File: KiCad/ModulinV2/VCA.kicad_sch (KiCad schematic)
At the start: 9 parts, among them IC20 AS3360D, U8 TL072HIDR

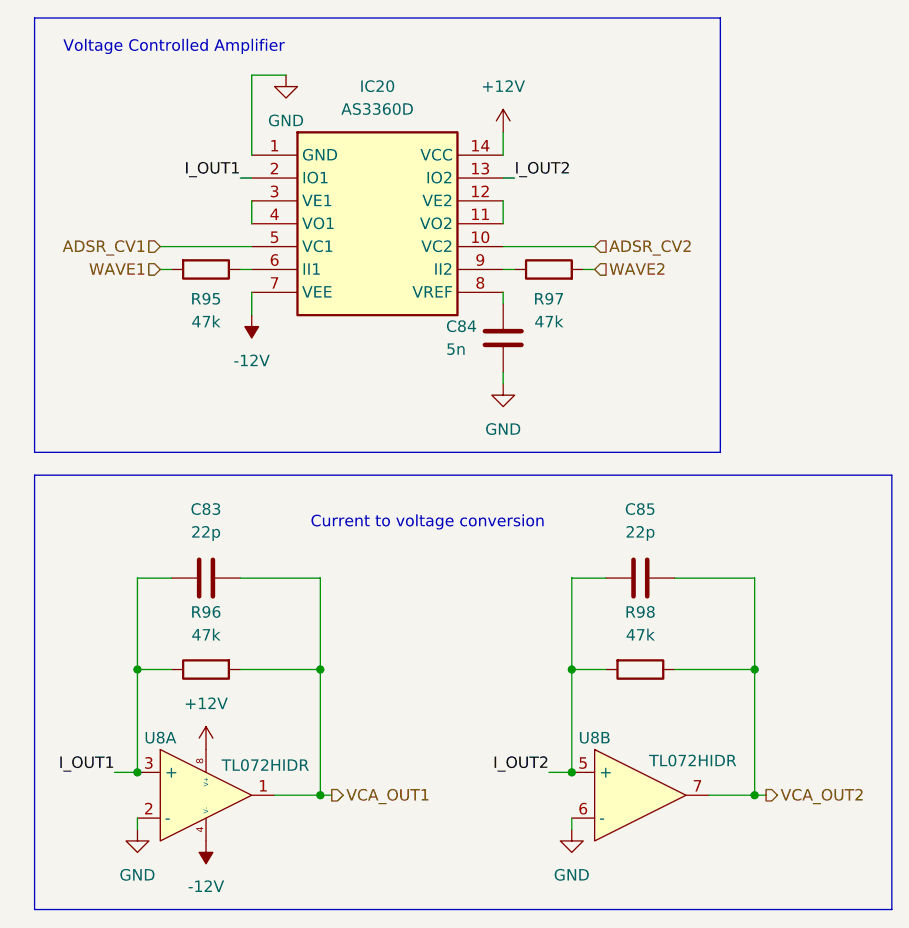
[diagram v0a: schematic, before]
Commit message: Fixed library issues and assigned most footprints
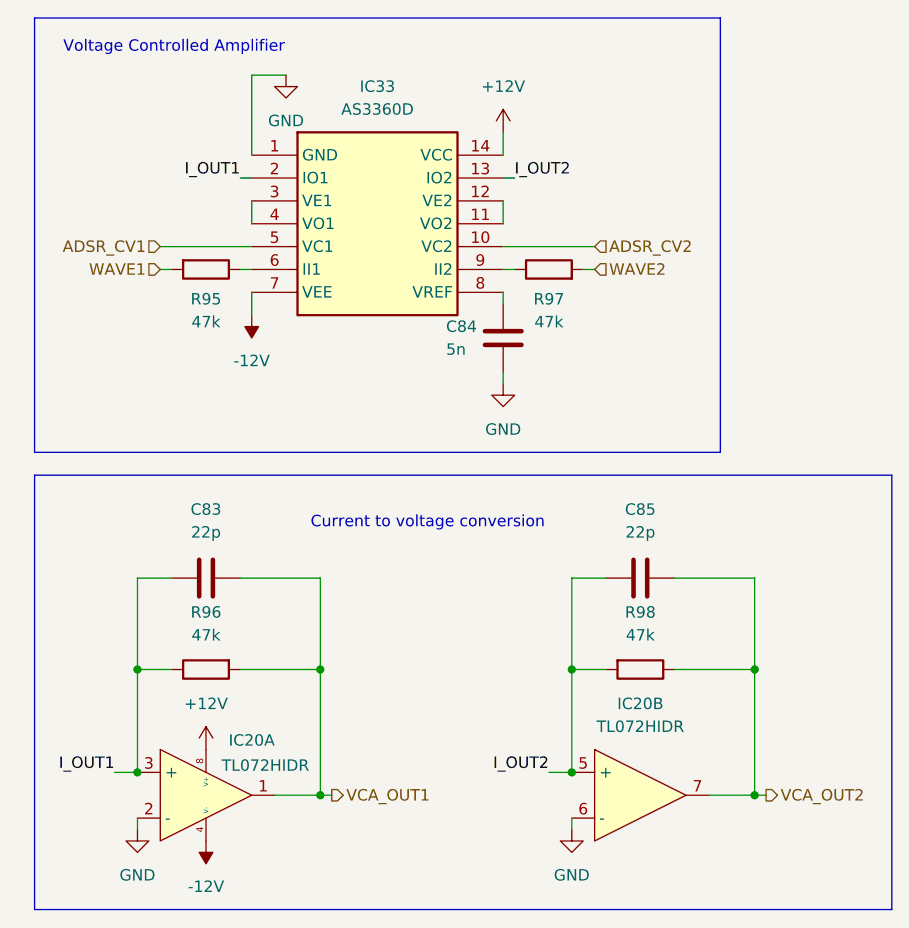
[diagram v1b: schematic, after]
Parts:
- removed IC20: AS3360D, SOIC127P620X175-14N, symbol AS3360D:AS3360D
- removed U8: TL072HIDR, symbol TL072HIDR:TL072HIDRx2
- added IC20: TL072HIDR, SamacSys_Parts:SOIC127P600X175-8N, symbol SamacSys_Parts:TL072HIDR
- added IC33: AS3360D, SamacSys_Parts:SOIC127P620X175-14N, symbol SamacSys_Parts:AS3360D
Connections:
- net +12V: now also IC20.8 (V+), IC33.14 (VCC)
- net -12V: now also IC20.4 (V-), IC33.7 (VEE)
- net ADSR_CV1: now also IC33.5 (VC1)
- net ADSR_CV2: now also IC33.10 (VC2)
- net GND: now also IC20.2 (-), IC20.6 (-), IC33.1 (GND)
- net I_OUT1: now also IC20.3 (+), IC33.2 (IO1)
- net I_OUT2: now also IC20.5 (+), IC33.13 (IO2)
- net VCA_OUT1: now also IC20.1
- net VCA_OUT2: now also IC20.7
- net at R97.1: now also IC33.9 (II2)
- net at R95.1: now also IC33.6 (II1)
- net at C84.1: now also IC33.8 (VREF)
- new net: IC33.11 (VO2), IC33.12 (VE2)
- new net: IC33.3 (VE1), IC33.4 (VO1)

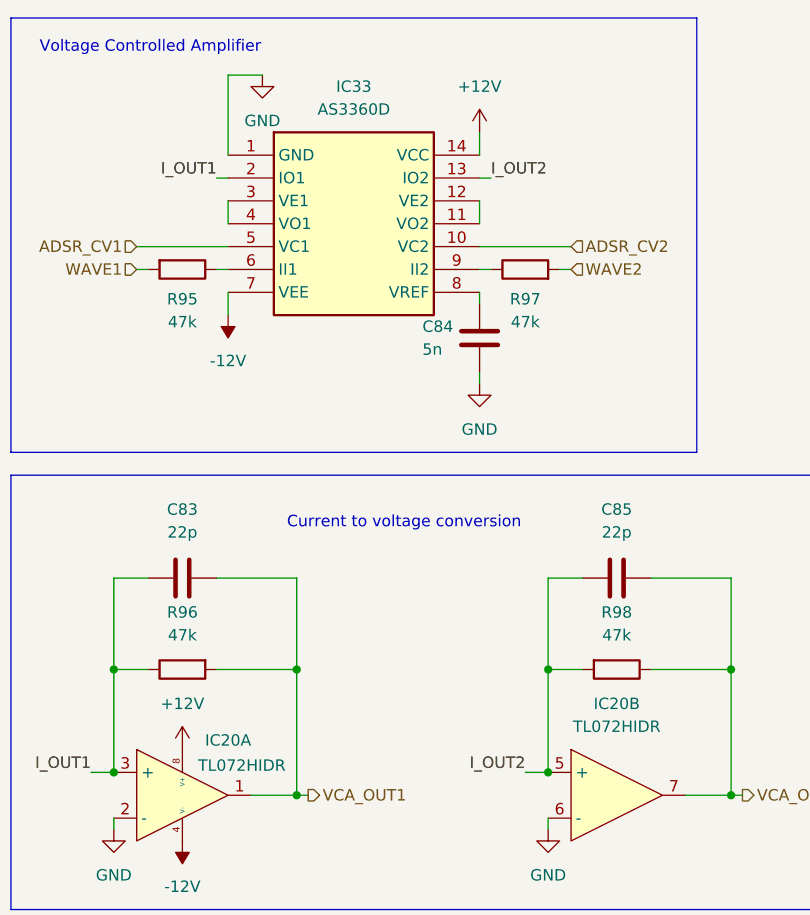
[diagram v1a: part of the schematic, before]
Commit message: Changed switch for the boot and nrst. Fixed the GATE interface trigger
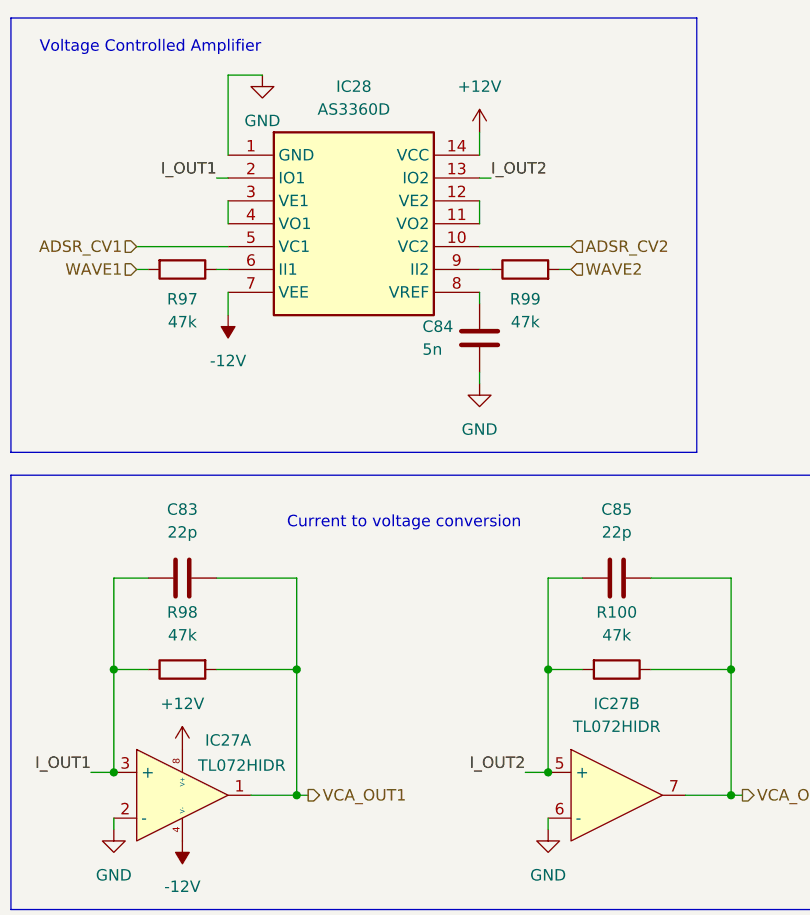
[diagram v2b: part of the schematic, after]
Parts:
- renumbered IC20 to IC27, IC33 to IC28, R98 to R100, R95 to R97, R96 to R98, R97 to R99
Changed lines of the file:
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@@
 		(dnp no)
 		(fields_autoplaced yes)
-		(property "Reference" "R98"
+		(property "Reference" "R100"
 			(at 81.28 80.01 90)
 			(effects
@@
 			(project "ModulinV2"
 				(path "/c6b34a57-3941-4b56-8b80-1848c7f41082/a5a8abcc-50bb-4382-96d0-cbdb724bb6e9"
-					(reference "R98")
+					(reference "R100")
 					(unit 1)
 				)
@@
 		(dnp no)
 		(fields_autoplaced yes)
-		(property "Reference" "#PWR0196"
+		(property "Reference" "#PWR0204"
 			(at 66.04 30.48 0)
 			(effects
@@
 			(project ""
 				(path "/c6b34a57-3941-4b56-8b80-1848c7f41082/a5a8abcc-50bb-4382-96d0-cbdb724bb6e9"
-					(reference "#PWR0196")
+					(reference "#PWR0204")
 					(unit 1)
 				)
@@
 		(on_board yes)
 		(dnp no)
-		(property "Reference" "R97"
+		(property "Reference" "R99"
 			(at 71.12 45.212 90)
 			(effects
@@
 			(project "ModulinV2"
 				(path "/c6b34a57-3941-4b56-8b80-1848c7f41082/a5a8abcc-50bb-4382-96d0-cbdb724bb6e9"
-					(reference "R97")
+					(reference "R99")
 					(unit 1)
 				)
@@
 		(dnp no)
 		(fields_autoplaced yes)
-		(property "Reference" "#PWR0192"
+		(property "Reference" "#PWR0200"
 			(at 33.02 99.06 0)
 			(effects
@@
 			(project "ModulinV2"
 				(path "/c6b34a57-3941-4b56-8b80-1848c7f41082/a5a8abcc-50bb-4382-96d0-cbdb724bb6e9"
-					(reference "#PWR0192")
+					(reference "#PWR0200")
 					(unit 1)
 				)
@@
 		(on_board yes)
 		(dnp no)
-		(property "Reference" "R95"
+		(property "Reference" "R97"
 			(at 33.02 45.212 90)
 			(effects
@@
 			(project "ModulinV2"
 				(path "/c6b34a57-3941-4b56-8b80-1848c7f41082/a5a8abcc-50bb-4382-96d0-cbdb724bb6e9"
-					(reference "R95")
+					(reference "R97")
 					(unit 1)
 				)
@@
 		(dnp no)
 		(fields_autoplaced yes)
-		(property "Reference" "#PWR0191"
+		(property "Reference" "#PWR0199"
 			(at 25.4 110.49 0)
 			(effects
@@
 			(project ""
 				(path "/c6b34a57-3941-4b56-8b80-1848c7f41082/a5a8abcc-50bb-4382-96d0-cbdb724bb6e9"
-					(reference "#PWR0191")
+					(reference "#PWR0199")
 					(unit 1)
 				)
@@
 		(dnp no)
 		(fields_autoplaced yes)
-		(property "Reference" "#PWR0197"
+		(property "Reference" "#PWR0205"
 			(at 66.04 60.96 0)
 			(effects
@@
 			(project ""
 				(path "/c6b34a57-3941-4b56-8b80-1848c7f41082/a5a8abcc-50bb-4382-96d0-cbdb724bb6e9"
-					(reference "#PWR0197")
+					(reference "#PWR0205")
 					(unit 1)
 				)
@@
 		(dnp no)
 		(fields_autoplaced yes)
-		(property "Reference" "#PWR0194"
+		(property "Reference" "#PWR0202"
 			(at 38.1 43.18 0)
 			(effects
@@
 			(project ""
 				(path "/c6b34a57-3941-4b56-8b80-1848c7f41082/a5a8abcc-50bb-4382-96d0-cbdb724bb6e9"
-					(reference "#PWR0194")
+					(reference "#PWR0202")
 					(unit 1)
 				)
@@
 		(dnp no)
 		(fields_autoplaced yes)
-		(property "Reference" "IC20"
+		(property "Reference" "IC27"
 			(at 81.28 90.17 0)
 			(effects
@@
 			(project ""
 				(path "/c6b34a57-3941-4b56-8b80-1848c7f41082/a5a8abcc-50bb-4382-96d0-cbdb724bb6e9"
-					(reference "IC20")
+					(reference "IC27")
 					(unit 2)
 				)
@@
 		(dnp no)
 		(fields_autoplaced yes)
-		(property "Reference" "#PWR0195"
+		(property "Reference" "#PWR0203"
 			(at 41.91 26.67 0)
 			(effects
@@
 			(project ""
 				(path "/c6b34a57-3941-4b56-8b80-1848c7f41082/a5a8abcc-50bb-4382-96d0-cbdb724bb6e9"
-					(reference "#PWR0195")
+					(reference "#PWR0203")
 					(unit 1)
 				)
@@
 		(dnp no)
 		(fields_autoplaced yes)
-		(property "Reference" "R96"
+		(property "Reference" "R98"
 			(at 33.02 80.01 90)
 			(effects
@@
 			(project ""
 				(path "/c6b34a57-3941-4b56-8b80-1848c7f41082/a5a8abcc-50bb-4382-96d0-cbdb724bb6e9"
-					(reference "R96")
+					(reference "R98")
 					(unit 1)
 				)
@@
 		(dnp no)
 		(fields_autoplaced yes)
-		(property "Reference" "IC33"
+		(property "Reference" "IC28"
 			(at 52.07 21.59 0)
 			(effects
@@
 			(project ""
 				(path "/c6b34a57-3941-4b56-8b80-1848c7f41082/a5a8abcc-50bb-4382-96d0-cbdb724bb6e9"
-					(reference "IC33")
+					(reference "IC28")
 					(unit 1)
 				)
@@
 		(on_board yes)
 		(dnp no)
-		(property "Reference" "IC20"
+		(property "Reference" "IC27"
 			(at 38.1 94.234 0)
 			(effects
@@
 			(project ""
 				(path "/c6b34a57-3941-4b56-8b80-1848c7f41082/a5a8abcc-50bb-4382-96d0-cbdb724bb6e9"
-					(reference "IC20")
+					(reference "IC27")
 					(unit 1)
 				)
@@
 		(dnp no)
 		(fields_autoplaced yes)
-		(property "Reference" "#PWR0193"
+		(property "Reference" "#PWR0201"
 			(at 33.02 101.6 0)
 			(effects
@@
 			(project "ModulinV2"
 				(path "/c6b34a57-3941-4b56-8b80-1848c7f41082/a5a8abcc-50bb-4382-96d0-cbdb724bb6e9"
-					(reference "#PWR0193")
+					(reference "#PWR0201")
 					(unit 1)
 				)
@@
 		(dnp no)
 		(fields_autoplaced yes)
-		(property "Reference" "#PWR0198"
+		(property "Reference" "#PWR0206"
 			(at 73.66 110.49 0)
 			(effects
@@
 			(project ""
 				(path "/c6b34a57-3941-4b56-8b80-1848c7f41082/a5a8abcc-50bb-4382-96d0-cbdb724bb6e9"
-					(reference "#PWR0198")
-					(unit 1)
-				)
+					(reference "#PWR0206")
+					(unit 1)
+				)

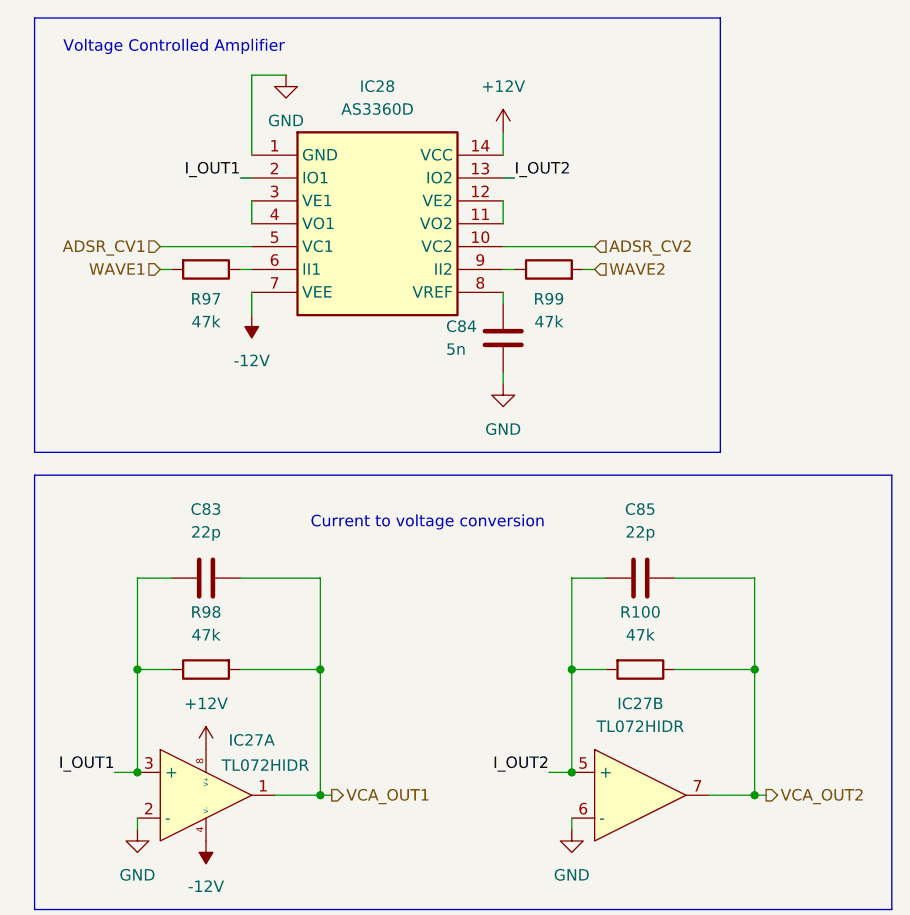
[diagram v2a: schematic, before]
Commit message: Started adding footprints for capacitors
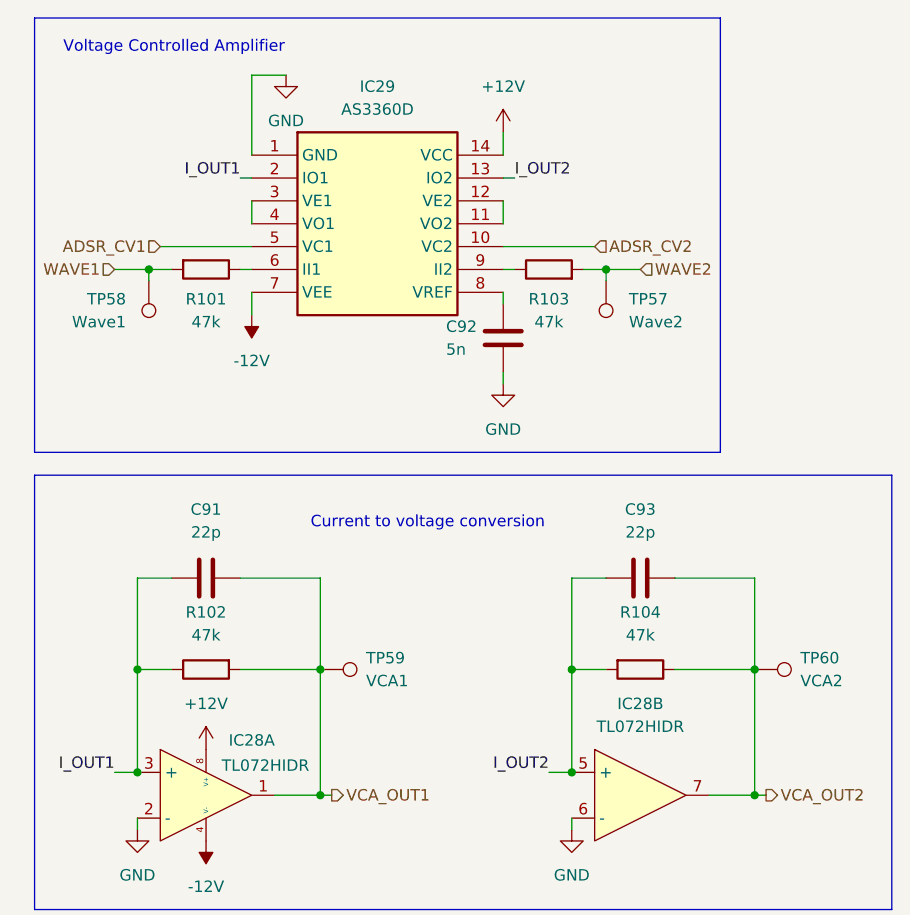
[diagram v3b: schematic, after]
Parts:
- added TP57: Wave2, SamacSys_Parts:TestPointLoop, symbol Connector:TestPoint
- added TP58: Wave1, SamacSys_Parts:TestPointLoop, symbol Connector:TestPoint
- added TP59: VCA1, SamacSys_Parts:TestPointLoop, symbol Connector:TestPoint
- added TP60: VCA2, SamacSys_Parts:TestPointLoop, symbol Connector:TestPoint
- renumbered C83 to C91, C84 to C92, C85 to C93, IC27 to IC28, IC28 to IC29, R97 to R101, R98 to R102, R99 to R103, R100 to R104
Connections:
- net VCA_OUT1: now also TP59.1
- net VCA_OUT2: now also TP60.1
- net WAVE1: now also TP58.1
- net WAVE2: now also TP57.1
